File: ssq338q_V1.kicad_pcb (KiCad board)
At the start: 6 copper layers, 32 x 40 mm, 127 parts, among them J4 Conn_01x04_MountingPin, J6 Conn_01x06_MountingPin, J7 Conn_01x03_MountingPin, J8 Conn_01x02_MountingPin, U1 TLV74018PDBVR, U11 W25Q128JVSIQ, U13 BL-M8812EU2, U14 TMI3411, U17 TMI3408F, U2 SSC338Q, U3 MP9943GQ-Z, U7 TMI3113B, X2 24MHz

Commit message: 22_09_26_23_16
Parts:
- removed RST1: ~, TestPoint:TestPoint_Pad_D1.0mm
- R67: moved to F.Cu
- moved R67 13.2 mm to (127.0, 110.8), turned to 90 degrees
- moved C168 3.81 mm to (132.3, 85.7), turned to 180 degrees
- moved C87 2.61 mm to (128.1, 90.2), turned to 0 degrees
- moved C153 2.28 mm to (128.4, 95.2), turned to -90 degrees
- moved C170 2.08 mm to (130.4, 85.7)
- moved C149 1.68 mm to (135.5, 102.5)
- moved C83 1.50 mm to (130.0, 84.1), turned to 0 degrees
- moved C161 1.33 mm to (128.3, 85.6)
- moved C173 1.33 mm to (128.3, 86.5)
- moved C85 1.15 mm to (122.9, 92.5)
- moved C160 1.04 mm to (129.3, 95.2), turned to -90 degrees
- moved C79 1.03 mm to (143.6, 86.1), turned to 180 degrees
- moved C41 1.01 mm to (124.8, 98.8), turned to 0 degrees
- moved R68 0.81 mm to (119.3, 98.5), turned to 0 degrees
- moved C155 0.76 mm to (129.8, 102.5)
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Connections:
- R67 pad 2: Net-(R67-Pad2) -> unconnected-(R67-Pad2)
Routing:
- net /GPIO0_LED1: track 0.00 -> 32.1 mm, vias 0 -> 2
- net +3V3: track 18.1 -> 46.3 mm, vias 18 -> 49
- net /SD_CDZ: track 0.00 -> 27.8 mm, vias 0 -> 2
- net /ETH_TX+: track 0.00 -> 21.5 mm, vias 0 -> 3
- net /ETH_TX-: track 0.00 -> 21.5 mm, vias 0 -> 3
- net /ETH_RX+: track 0.00 -> 20.8 mm, vias 0 -> 2
- net +1V0: track 4.95 -> 25.8 mm, vias 0 -> 12
- net /ETH_RX-: track 0.00 -> 20.4 mm, vias 0 -> 2
- net /UART_RX1: track 0.00 -> 20.1 mm, vias 0 -> 2
- net /UART_TX1: track 0.00 -> 16.6 mm, vias 0 -> 2
- net /SPI_WPZ: track 0.00 -> 15.0 mm, vias 0 -> 2
- net /SD_DATA1: track 0.00 -> 14.0 mm
- net /SPI_SDO: track 0.00 -> 13.3 mm, vias 0 -> 2
- net /SD_DATA0: track 0.00 -> 13.2 mm
- net /SD_DATA2: track 0.00 -> 12.4 mm
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- added copper zone on In1.Cu, net GND

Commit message: 24_09_26
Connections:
- net /USB_DM renamed /USB_DN
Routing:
- net +1V8: track 5.17 -> 69.8 mm, vias 3 -> 9
- net +1V0: track 25.8 -> 86.2 mm, vias 12 -> 20
- net +1V5: track 15.4 -> 46.9 mm, vias 21 -> 15
- net /USB_DN: track 0.00 -> 26.9 mm, vias 0 -> 1
- net /USB_DP: track 0.00 -> 26.5 mm, vias 0 -> 1
- net GND: track 5.05 -> 13.6 mm, vias 126 -> 116
- net /GPIO0_LED1: track 32.1 -> 35.9 mm
- net +3V3: vias 49 -> 48
- added copper zone on In3.Cu, net +1V0
- added copper zone on F.Cu, net +1V8
- added copper zone on In3.Cu, net +1V8
- added copper zone on In3.Cu, net +3V3
- added copper zone on In4.Cu, net GND

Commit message: minor changes
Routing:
- net GND: track 13.6 -> 19.4 mm, vias 116 -> 126
- net VBUS: vias 19 -> 11
- net +3V3: vias 48 -> 42

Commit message: traces done
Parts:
- moved C159 0.43 mm to (118.2, 110.4)
- moved R48 0.10 mm to (144.9, 102.5)
- moved R62 0.10 mm to (144.0, 102.5)
- moved C41 0.08 mm to (124.8, 98.8)
- moved C82 0.05 mm to (143.1, 102.5)
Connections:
- J4 pad 3: /UART_RX1 -> /FUART_RX
- J4 pad 4: /UART_TX1 -> /FUART_TX
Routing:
- net GND: track 19.4 -> 76.2 mm, vias 126 -> 177
- net /FUART_RX: track 0.00 -> 33.8 mm, vias 0 -> 2
- net /FUART_TX: track 0.00 -> 30.4 mm, vias 0 -> 2
- net /UART_RX1: track 20.1 -> 0.00 mm, vias 2 -> 0
- net /UART_TX1: track 16.6 -> 0.00 mm, vias 2 -> 0
- net /USB_DP: track 26.5 -> 22.5 mm
- net +1V8: track 69.8 -> 65.9 mm, vias 9 -> 8
- net /USB_DN: track 26.9 -> 23.2 mm
- net +5V: track 14.9 -> 18.1 mm, vias 42 -> 36
- net +1V0: track 86.2 -> 84.4 mm
- net +1V5: track 46.9 -> 45.7 mm, vias 15 -> 13
- net /POWER/3V3EN: track 6.56 -> 6.44 mm, vias 1 -> 0
- net +3V3: track 46.3 -> 46.4 mm, vias 42 -> 43
- net VBUS: vias 11 -> 12
- net /ETH_TX-: vias 3 -> 2
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- added copper zone on In3.Cu, net +1V5
- added copper zone on F.Cu, net GND
- added copper zone on In2.Cu, net GND

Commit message: minor changes
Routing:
- net +3V3: track 46.4 -> 47.4 mm, vias 43 -> 36
- net GND: track 76.2 -> 76.1 mm, vias 177 -> 176
- net +5V: vias 36 -> 27

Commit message: pcb finalized
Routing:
- net +1V0: track 84.4 -> 83.4 mm, vias 20 -> 19
- net GND: vias 176 -> 200
- net +5V: vias 27 -> 25

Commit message: minor changes and prepared BOM
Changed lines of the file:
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@@
 	)
 	(via
-		(at 126.83 120.15)
+		(at 126.83 120.05)
 		(size 0.6)
 		(drill 0.3)
@@
 	)
 	(via
-		(at 128.31 120.15)
+		(at 128.31 120.05)
 		(size 0.6)
 		(drill 0.3)
@@
 	)
 	(via
-		(at 125.35 120.15)
+		(at 125.35 120.05)
 		(size 0.6)
 		(drill 0.3)
@@
 	)
 	(via
-		(at 124.61 120.15)
+		(at 124.61 120.05)
 		(size 0.6)
 		(drill 0.3)
@@
 	)
 	(via
-		(at 126.09 120.15)
+		(at 126.09 120.05)
 		(size 0.6)
 		(drill 0.3)
@@
 	)
 	(via
-		(at 127.57 120.15)
+		(at 127.57 120.05)
 		(size 0.6)
 		(drill 0.3)
@@
 				(xy 137.84 108.3) (xy 137.85 111.2) (xy 140.477841 111.19544) (xy 140.48 112.44) (xy 140.48 113.344999)
 				(xy 144.34 113.354999) (xy 144.34 114.79) (xy 138.171891 114.80028) (xy 138.168125 116.870368) (xy 139.437475 117.505561)
-				(xy 140.89674 118.524815) (xy 141.7846 118.855605) (xy 141.75 120.55) (xy 134.75 120.55) (xy 124.25 120.55)
-				(xy 124.248923 118.802743) (xy 128.6 118.800062) (xy 128.6 119.65) (xy 134.75 119.65) (xy 134.75 115.45)
-				(xy 134.2 115.45) (xy 134.2 113.9) (xy 135.75 113.9) (xy 135.85381 119.35) (xy 138.476563 119.35)
-				(xy 138.424209 117.674736) (xy 137.45 117.35) (xy 137.45 116.871306) (xy 137.45 116.87076) (xy 137.45 116.87)
-				(xy 137.45 114.108432) (xy 138.908205 113.492327) (xy 138.91393 112.05) (xy 137.9 112.05) (xy 136.95 112.05)
-				(xy 136.95 110) (xy 135.65 110) (xy 135.66 109.22) (xy 136.77 109.22) (xy 136.78 108.29)
+				(xy 140.89674 118.524815) (xy 141.7846 118.855605) (xy 141.75 120.55) (xy 134.75 120.55) (xy 134.750278 120.55)
+				(xy 134.749722 119.65) (xy 134.75 119.65) (xy 134.75 115.45) (xy 134.2 115.45) (xy 134.2 113.9)
+				(xy 135.75 113.9) (xy 135.85381 119.35) (xy 138.476563 119.35) (xy 138.424209 117.674736) (xy 137.45 117.35)
+				(xy 137.45 116.871306) (xy 137.45 116.87076) (xy 137.45 116.87) (xy 137.45 114.108432) (xy 138.908205 113.492327)
+				(xy 138.91393 112.05) (xy 137.9 112.05) (xy 136.95 112.05) (xy 136.95 110) (xy 135.65 110) (xy 135.66 109.22)
+				(xy 136.77 109.22) (xy 136.78 108.29)
 			)
 		)

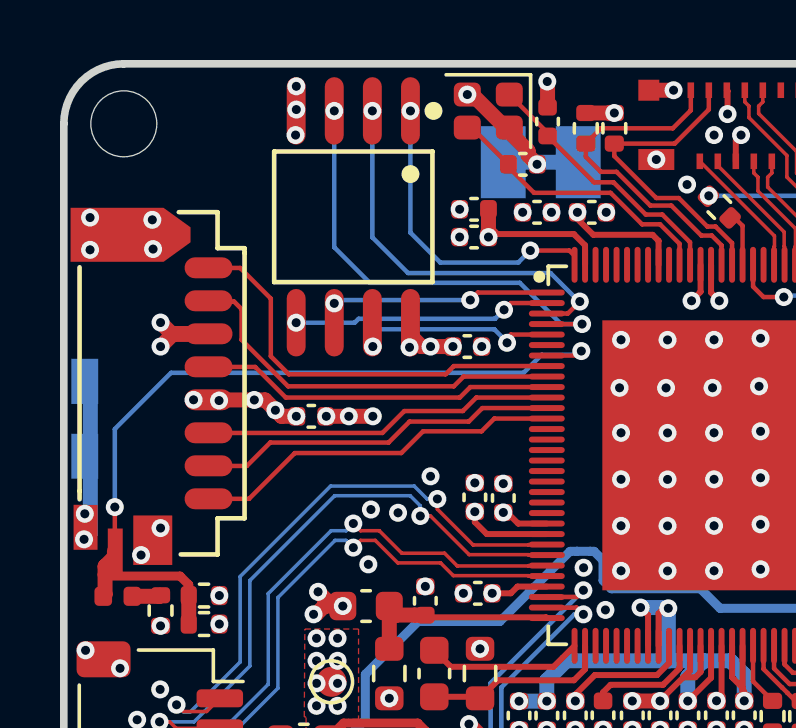
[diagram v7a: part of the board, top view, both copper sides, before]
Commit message: sd pullup, finilized design
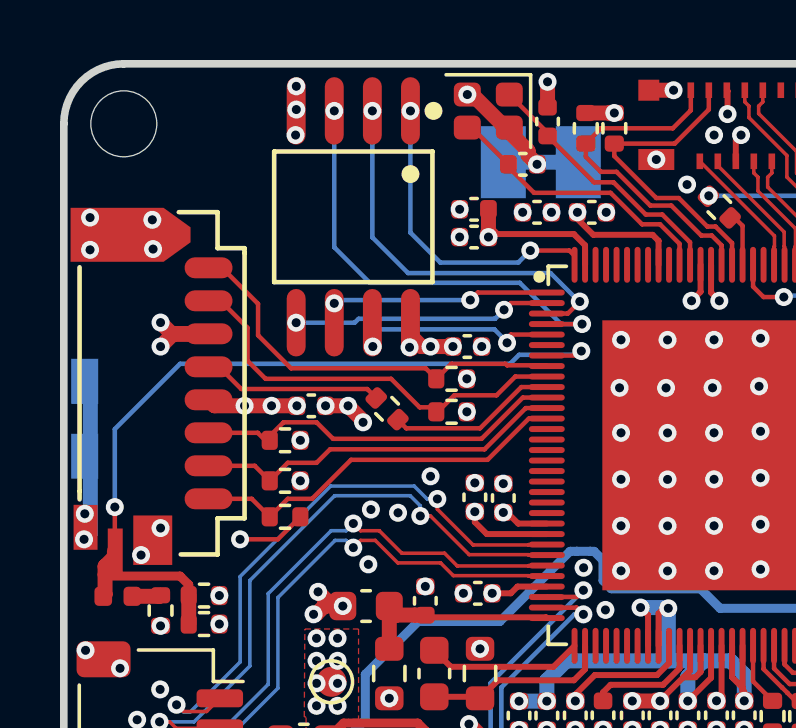
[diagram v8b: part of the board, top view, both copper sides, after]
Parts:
- added R50: 4k7, Resistor_SMD:R_0402_1005Metric, F.Cu at (122.0, 95.8)
- added R51: 4k7, Resistor_SMD:R_0402_1005Metric, F.Cu at (122.0, 94.7)
- added R52: 4k7, Resistor_SMD:R_0402_1005Metric, F.Cu at (127.6, 92.3)
- added R53: 4k7, Resistor_SMD:R_0402_1005Metric, F.Cu at (122.0, 93.3)
- added R54: 4k7, Resistor_SMD:R_0402_1005Metric, F.Cu at (127.6, 91.2)
- added R55: 22, Resistor_SMD:R_0402_1005Metric, F.Cu at (125.5, 92.2)
- R15, R23: value 100K -> 100k
- R21, R22, R38, R65, R74: value 10K -> 10k
- R36: value 75K -> 75k
- R37: value 15K -> 15k
- moved C85 0.35 mm to (122.9, 92.2)
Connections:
- U2 pad 10: /SD_CLK -> Net-(U2-SD0_CLK)
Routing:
- net /SD_CLK: track 11.9 -> 6.02 mm
- net Net-(U2-SD0_CLK): track 0.00 -> 5.66 mm
- net +3V3: track 47.4 -> 49.6 mm, vias 36 -> 39
- net /SD_CMD: track 11.8 -> 12.6 mm
- net /SD_DATA0: track 13.2 -> 14.0 mm
